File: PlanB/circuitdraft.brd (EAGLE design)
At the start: 24 x 43 mm, 20 parts, among them Q1 16 MHz

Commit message: added biggnd and bigpower for large traces
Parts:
- added BRIDGE1, BRIDGE2, BRIDGE3: (no value), rcl:M0805
- moved CHARGER 3.70 mm to (16.6, 35.1)
- moved LED 2.00 mm to (23.2, 29.6)
- moved BUTTON 1.80 mm to (23.2, 33.5)
- turned SERVO1 to 180 degrees
- turned SERVO2 to 180 degrees
- turned SERVO3 to 180 degrees
- turned SERVO4 to 180 degrees
- turned SERVO5 to 180 degrees
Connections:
- new net BIGGND: BRIDGE3.1, CHARGER.3, REGIN.2, REGOUT.3, SERVO1.3, SERVO2.3, SERVO3.3, SERVO4.3, SERVO5.3
- new net BIGPOWER: BRIDGE1.1, REGOUT.2, SERVO1.2, SERVO2.2, SERVO3.2, SERVO4.2, SERVO5.2
- new net N$9: BRIDGE2.2, U$1.36
- net GND: now also BRIDGE3.2; no longer CHARGER.3, REGIN.2, REGOUT.3, SERVO1.3, SERVO2.3, SERVO3.3, SERVO4.3, SERVO5.3
- net POWER: now also BRIDGE1.2; no longer REGOUT.2, SERVO1.2, SERVO2.2, SERVO3.2, SERVO4.2, SERVO5.2
- net VBAT: now also BRIDGE2.1; no longer U$1.36
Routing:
- net BIGGND: track 0.00 -> 79.7 mm
- net BIGPOWER: track 0.00 -> 55.7 mm, vias 0 -> 1
- net INTERRUPT: track 18.7 -> 54.2 mm, vias 0 -> 2
- net POWER: track 88.8 -> 56.9 mm, vias 1 -> 0
- net SIGNAL3: track 49.7 -> 28.8 mm, vias 0 -> 1
- net SIGNAL2: track 57.7 -> 37.5 mm
- net VBUS: track 21.8 -> 40.0 mm, vias 1 -> 2
- net N$9: track 0.00 -> 7.01 mm
- net DATAIN: track 23.6 -> 18.2 mm
- net RST: track 14.0 -> 19.1 mm, vias 0 -> 3
- net GND: track 0.00 -> 4.90 mm
- net SIGNAL4: track 45.9 -> 50.7 mm
- net SIGNAL5: track 23.4 -> 19.1 mm, vias 1 -> 2
- net N$2: track 6.57 -> 9.69 mm
- net SCK: track 12.4 -> 15.2 mm
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
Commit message: more ajustments
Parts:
- removed BRIDGE3: (no value), rcl:M0805
- removed Q1: 16 MHz, crystal:HC49U
- removed REGIN, REGOUT: (no value), pinhead:1X03
- added REGGNDIN, REGGNDOUT, REGVIN, REGVOUT: (no value), pinhead:1X01
- added Y1: CY16BPS, SamacSys_Parts:CY16BPS
- moved R1 18.3 mm to (19.2, 35.8), turned to 270 degrees
- moved R2 17.9 mm to (16.6, 35.5), turned to 270 degrees
- moved USB 17.7 mm to (7.37, 37.0)
- moved C1 15.6 mm to (16.6, 27.6), turned to 0 degrees
- moved C3 15.3 mm to (27.4, 12.5), turned to 180 degrees
- moved BRIDGE2 13.4 mm to (14.5, 40.3), turned to 270 degrees
- moved BRIDGE1 12.1 mm to (28.4, 2.80), turned to 90 degrees
- moved SERVO1 11.1 mm to (9.60, 28.9)
- moved SERVO2 11.1 mm to (9.60, 25.6)
- moved SERVO3 11.1 mm to (9.60, 22.4)
- moved SERVO4 11.1 mm to (9.60, 19.1)
- moved SERVO5 11.1 mm to (9.60, 15.8)
- moved CHARGER 5.44 mm to (11.5, 37.0)
- moved LED 3.26 mm to (25.3, 27.1), turned to 315 degrees
- moved C2 1.78 mm to (28.6, 7.78)
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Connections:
- removed net BIGGND: BRIDGE3.1, CHARGER.3, REGIN.2, REGOUT.3, SERVO1.3, SERVO2.3, SERVO3.3, SERVO4.3, SERVO5.3
- net BIGPOWER: now also REGVOUT.1; no longer REGOUT.2
- net GND: now also CHARGER.3, REGGNDIN.1, REGGNDOUT.1, SERVO1.3, SERVO2.3, SERVO3.3, SERVO4.3, SERVO5.3, U$1.15, U$1.35, U$1.43; no longer BRIDGE3.2
- net N$5: now also C2.2, U$1.17, Y1.2; no longer C3.2, Q1.1, U$1.16
- net N$6: now also C3.2, U$1.16, Y1.1; no longer C2.2, Q1.3, U$1.17
- net POWER: now also U$1.2
- net VBAT: now also REGVIN.1; no longer REGIN.1
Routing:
- net BIGGND: track 79.7 -> 0.00 mm
- net SIGNAL4: track 50.7 -> 13.6 mm, vias 1 -> 0
- net INTERRUPT: track 54.2 -> 29.4 mm, vias 2 -> 0
- net SIGNAL2: track 37.5 -> 14.6 mm, vias 2 -> 0
- net BIGPOWER: track 55.7 -> 38.9 mm, vias 1 -> 0
- net SIGNAL1: track 38.2 -> 21.5 mm, vias 1 -> 0
- net SIGNAL3: track 28.8 -> 13.4 mm
- net N$4: track 3.67 -> 18.5 mm, vias 0 -> 1
- net POWER: track 56.9 -> 69.8 mm, vias 0 -> 2
- net VBUS: track 40.0 -> 29.8 mm, vias 2 -> 0
- net MISO: track 9.74 -> 19.2 mm, vias 1 -> 0
- net N$9: track 7.01 -> 16.4 mm, vias 0 -> 2
- net N$1: track 26.0 -> 35.4 mm, vias 3 -> 1
- net VBAT: track 26.9 -> 17.7 mm
- net N$2: track 9.69 -> 18.5 mm, vias 0 -> 1
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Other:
- board size 24 x 43 mm -> 25 x 43 mm

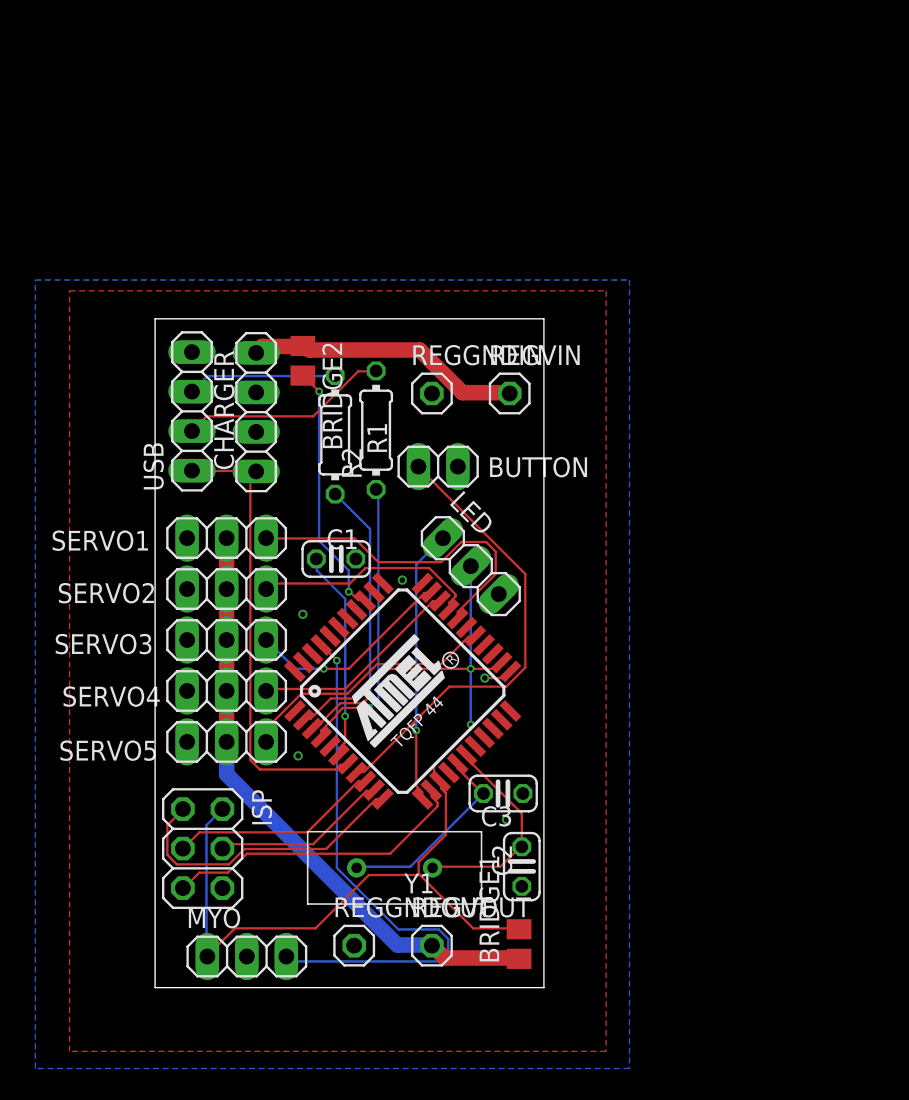
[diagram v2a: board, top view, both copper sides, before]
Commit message: refined board and fixed locations and orintations
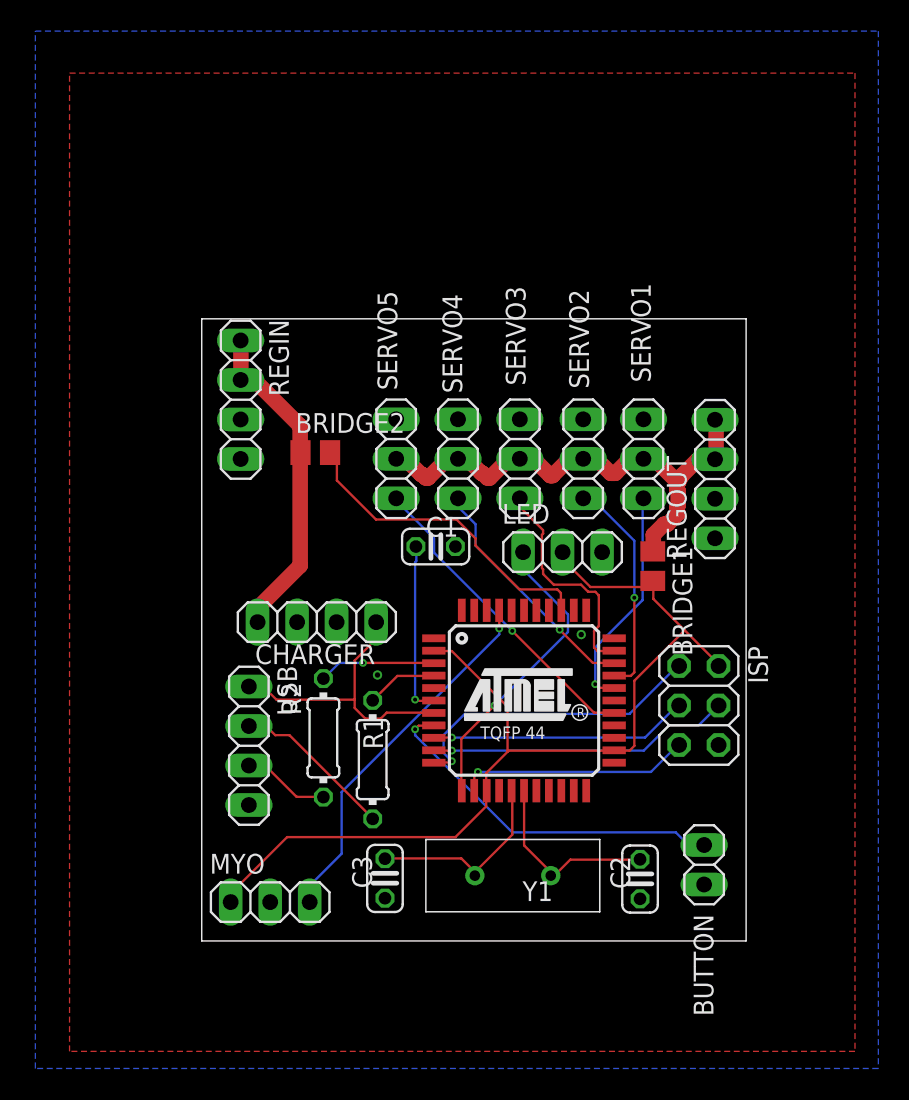
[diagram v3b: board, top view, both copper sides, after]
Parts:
- removed REGGNDIN, REGGNDOUT, REGVIN, REGVOUT: (no value), pinhead:1X01
- added REGIN, REGOUT: (no value), pinhead:1X04
- moved ISP 33.2 mm to (40.0, 18.1)
- moved BUTTON 30.8 mm to (40.3, 7.90), turned to 270 degrees
- moved SERVO1 27.3 mm to (36.4, 34.0), turned to 90 degrees
- moved BRIDGE1 25.8 mm to (37.0, 27.1), turned to 270 degrees
- moved SERVO2 24.4 mm to (32.5, 34.0), turned to 90 degrees
- moved SERVO3 22.2 mm to (28.4, 34.0), turned to 90 degrees
- moved USB 21.8 mm to (11.0, 15.6), turned to 270 degrees
- moved SERVO5 21.2 mm to (20.5, 34.0), turned to 90 degrees
- moved R1 21.2 mm to (19.0, 14.7), turned to 90 degrees
- moved SERVO4 21.1 mm to (24.5, 34.0), turned to 90 degrees
- moved R2 19.5 mm to (15.8, 16.1), turned to 90 degrees
- moved CHARGER 14.1 mm to (15.4, 23.5), turned to 180 degrees
- moved C3 9.36 mm to (19.8, 7.02), turned to 90 degrees
- moved U$1 7.82 mm to (28.7, 18.5), turned to 0 degrees
- moved C2 7.64 mm to (36.2, 6.98)
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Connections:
- net BIGPOWER: now also REGOUT.3, REGOUT.4; no longer REGVOUT.1
- net GND: now also REGIN.3, REGIN.4, REGOUT.1, REGOUT.2; no longer REGGNDIN.1, REGGNDOUT.1
- net VBAT: now also REGIN.1, REGIN.2; no longer REGVIN.1
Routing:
- net N$4: track 18.5 -> 4.58 mm, vias 1 -> 0
- net N$1: track 35.4 -> 23.8 mm
- net VBUS: track 29.8 -> 18.8 mm
- net N$2: track 18.5 -> 7.52 mm
- net MOSI: track 11.3 -> 19.5 mm, vias 0 -> 1
- net SIGNAL1: track 21.5 -> 14.6 mm, vias 0 -> 1
- net INTERRUPT: track 29.4 -> 23.2 mm, vias 0 -> 1
- net BIGPOWER: track 38.9 -> 33.4 mm
- net POWER: track 69.8 -> 64.3 mm, vias 2 -> 0
- net RST: track 19.8 -> 15.0 mm, vias 0 -> 1
- net N$9: track 16.4 -> 20.8 mm, vias 2 -> 0
- net D-: track 9.63 -> 5.63 mm
- net VBAT: track 17.7 -> 21.4 mm
- net SIGNAL5: track 16.7 -> 20.4 mm, vias 0 -> 1
- net SCK: track 13.5 -> 16.7 mm, vias 0 -> 1
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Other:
- board size 25 x 43 mm -> 35 x 40 mm

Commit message: final refinement
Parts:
- C1: device rcl:C025-024X044 -> rcl:C050-024X044
- R1, R2: device rcl:0204/7 -> rcl:0207/10
- moved C1 1.20 mm to (22.2, 27.5)
- moved R1 0.92 mm to (18.8, 15.6)
- moved U$1 0.80 mm to (27.9, 18.5)
- moved R2 0.50 mm to (15.8, 15.6)
- moved BRIDGE1 0.36 mm to (37.3, 26.9)
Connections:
- net INTERRUPT: now also U$1.1; no longer U$1.8
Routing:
- net INTERRUPT: track 23.2 -> 30.9 mm
- net MOSI: track 19.5 -> 23.7 mm
- net VBUS: track 18.8 -> 22.5 mm
- net DATAIN: track 19.4 -> 22.2 mm
- net SCK: track 16.7 -> 17.8 mm
- net N$9: track 20.8 -> 19.7 mm
- net N$4: track 4.58 -> 3.59 mm
- net RST: track 15.0 -> 15.9 mm
- net POWER: track 64.3 -> 63.6 mm
- net D-: track 5.63 -> 6.37 mm
- net SIGNAL3: track 14.6 -> 13.9 mm
- net SIGNAL1: track 14.6 -> 13.9 mm
- net SIGNAL4: track 15.6 -> 15.0 mm
- net N$2: track 7.52 -> 7.16 mm, vias 1 -> 0
- net MISO: track 20.1 -> 20.4 mm, vias 1 -> 2

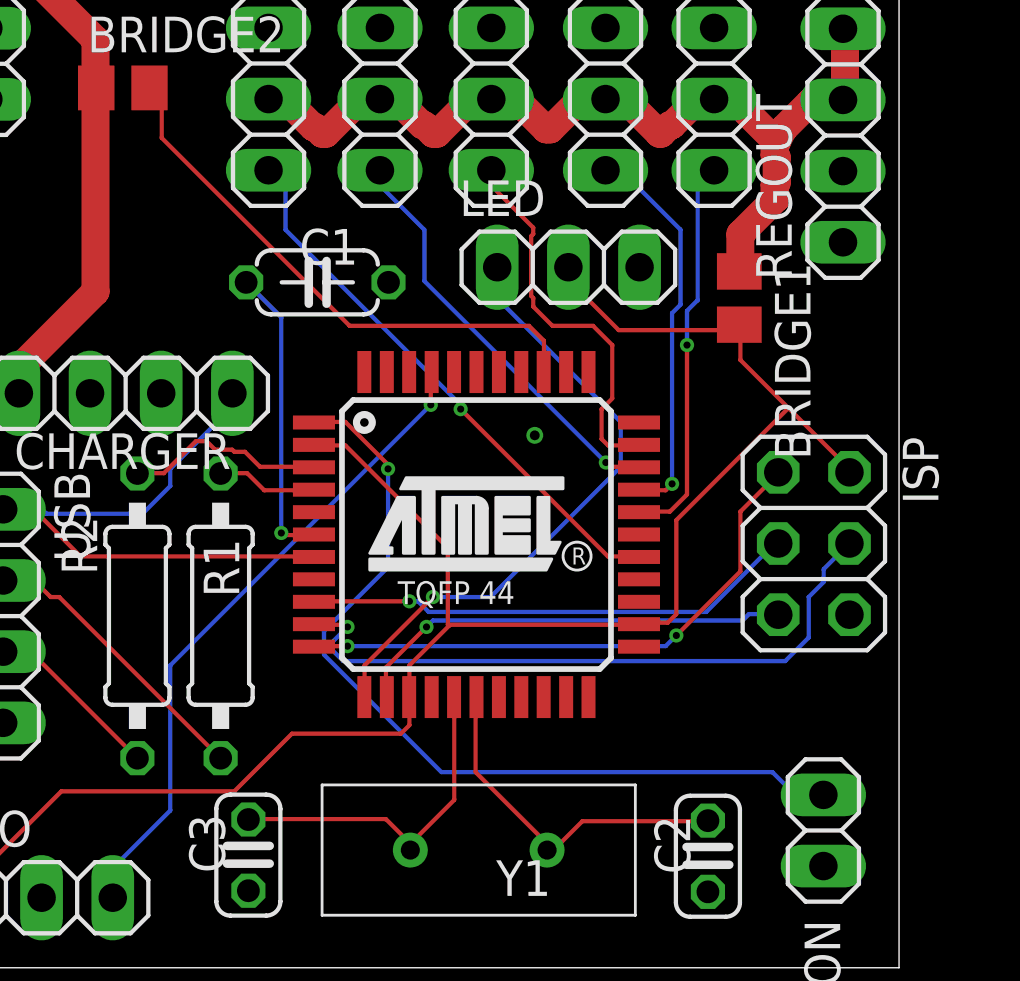
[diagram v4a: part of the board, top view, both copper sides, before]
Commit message: changed some pins to match arduino pins
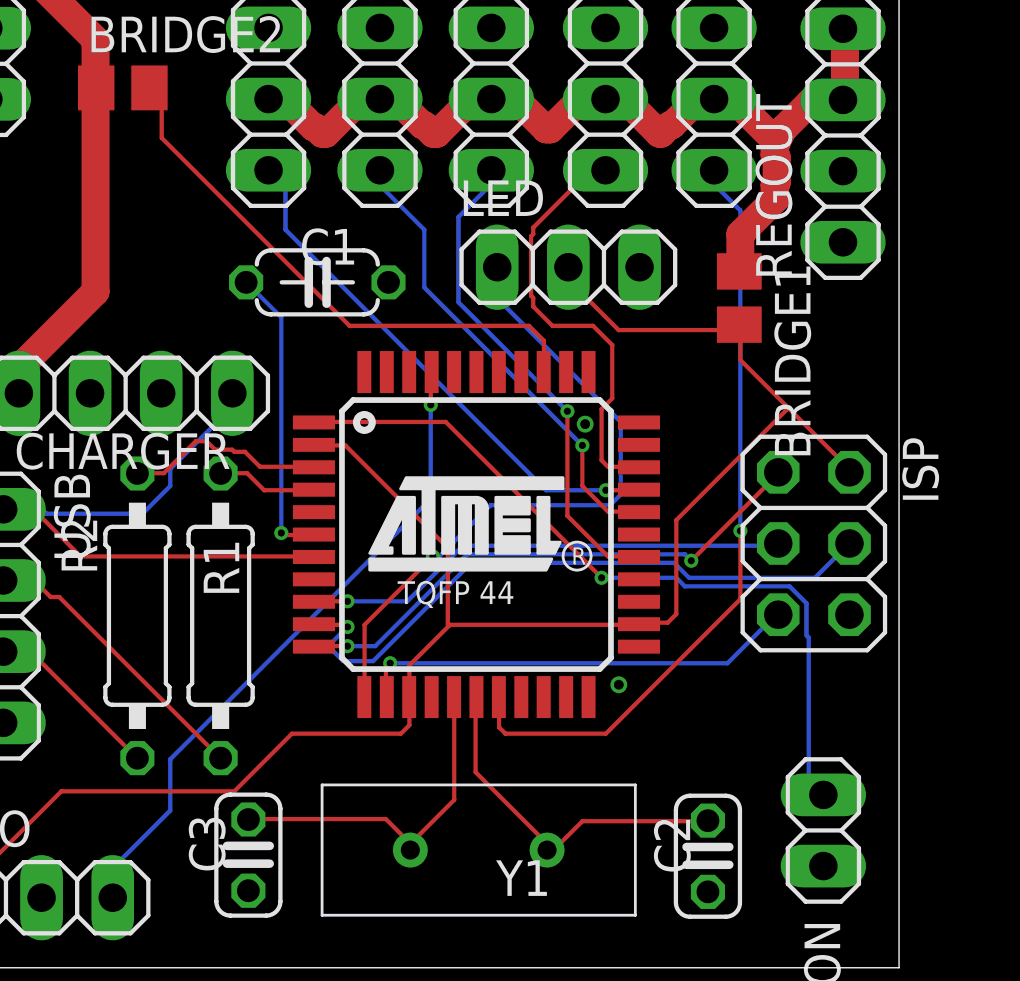
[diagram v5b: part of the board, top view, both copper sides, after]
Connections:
- removed net INT: U$1.25
- removed net SCL: U$1.18
- removed net SDA: U$1.19
- removed net STAT: U$1.26
- net SIGNAL1: now also U$1.18; no longer U$1.29
- net SIGNAL2: now also U$1.31; no longer U$1.30
- net SIGNAL3: now also U$1.27; no longer U$1.32
- net SIGNAL4: now also U$1.29; no longer U$1.31
- net SIGNAL5: now also U$1.30; no longer U$1.27
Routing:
- net SIGNAL1: track 13.9 -> 27.5 mm
- net SIGNAL3: track 13.9 -> 17.6 mm, vias 0 -> 1
- net INTERRUPT: track 30.9 -> 27.4 mm
- net SIGNAL4: track 15.0 -> 16.7 mm
- net DATAIN: track 22.2 -> 23.6 mm
- net SIGNAL2: track 14.1 -> 15.4 mm, vias 1 -> 0
- net SIGNAL5: track 19.9 -> 18.8 mm
- net MISO: track 20.4 -> 19.4 mm
- net MOSI: track 23.7 -> 23.1 mm

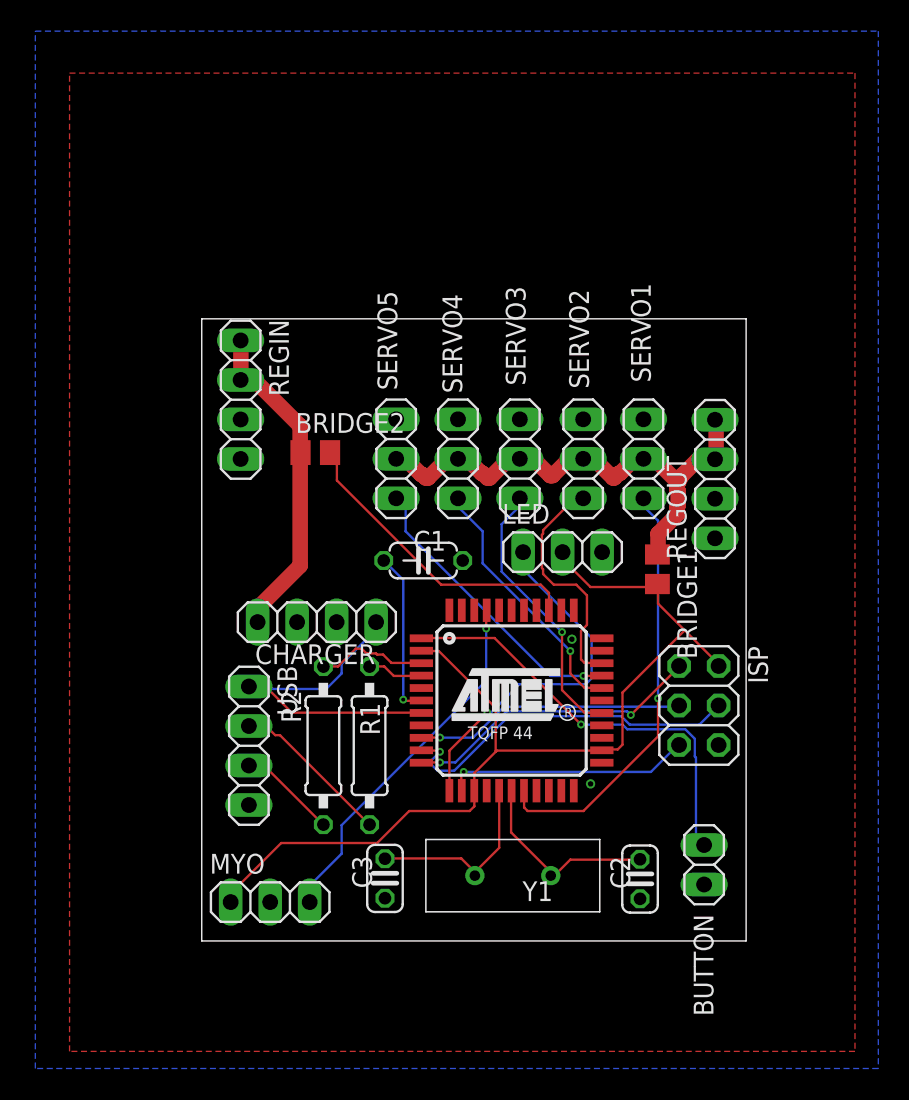
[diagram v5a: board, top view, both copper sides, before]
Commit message: updated
rotated servo ports
removed unnecessary USB things
moved some things around
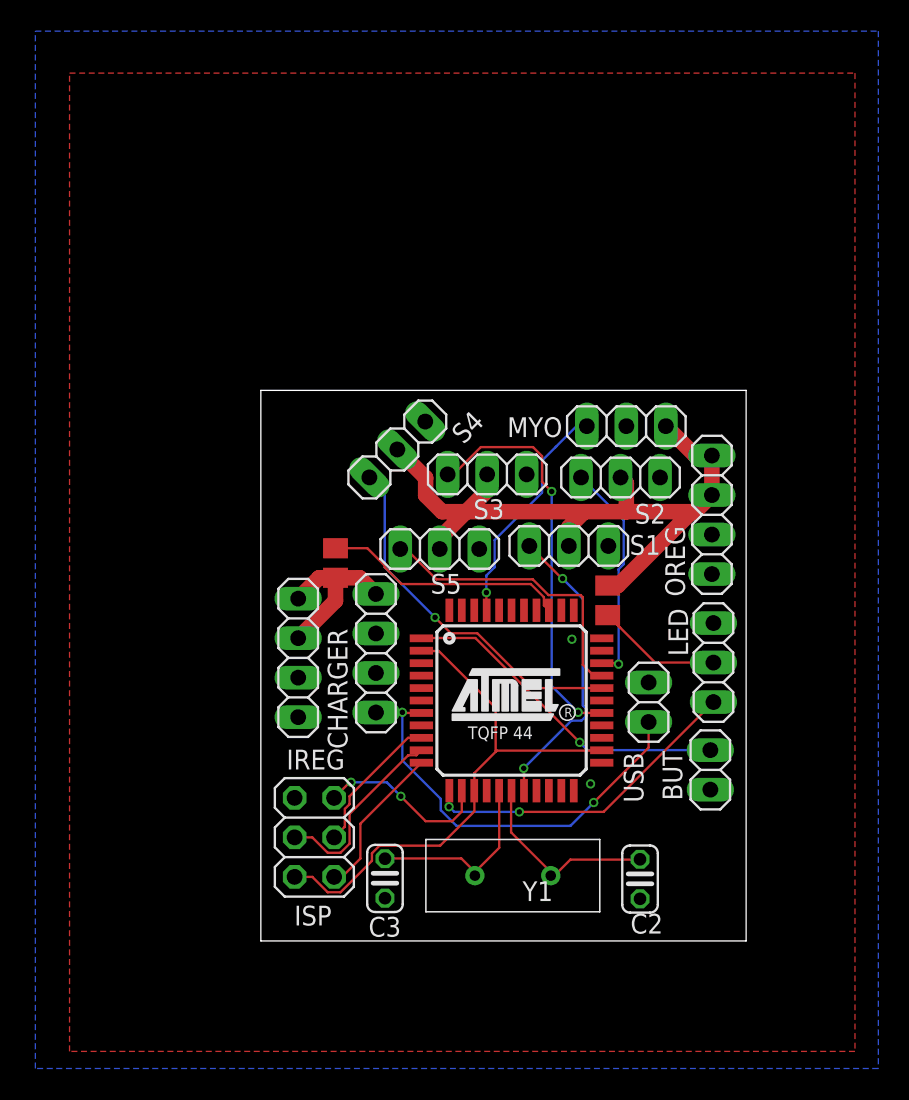
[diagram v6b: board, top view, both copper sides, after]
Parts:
- removed BUTTON: (no value), pinhead:1X02
- removed C1: 1 uF, rcl:C050-024X044
- removed R1, R2: 22 Ohms, rcl:0207/10
- removed REGIN, REGOUT: (no value), pinhead:1X04
- removed SERVO1, SERVO2, SERVO3, SERVO4, SERVO5: (no value), pinhead:1X03
- added BUT: (no value), pinhead:1X02
- added IREG, OREG: (no value), pinhead:1X04
- added S1, S2, S3, S4, S5: (no value), pinhead:1X03
- USB: device pinhead:1X04 -> pinhead:1X02
- moved MYO 38.2 mm to (35.3, 36.1), turned to 180 degrees
- moved ISP 26.1 mm to (15.2, 9.66), turned to 90 degrees
- moved USB 25.9 mm to (36.7, 18.4), turned to 90 degrees
- moved LED 12.0 mm to (40.9, 20.9), turned to 90 degrees
- moved BRIDGE2 7.22 mm to (16.6, 27.3), turned to 90 degrees
- moved CHARGER 4.29 mm to (19.2, 21.5), turned to 90 degrees
- moved BRIDGE1 3.77 mm to (34.1, 24.9)
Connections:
- removed net D+: R1.1, USB.2
- removed net D-: R2.1, USB.3
- removed net N$2: R2.2, U$1.3
- removed net N$3: C1.1, U$1.6
- removed net N$4: R1.2, U$1.4
- net BIGPOWER: now also MYO.1, OREG.3, OREG.4, S1.2, S2.2, S3.2, S4.2, S5.2; no longer REGOUT.3, REGOUT.4, SERVO1.2, SERVO2.2, SERVO3.2, SERVO4.2, SERVO5.2
- net GND: now also BUT.2, IREG.3, IREG.4, OREG.1, OREG.2, S1.3, S2.3, S3.3, S4.3, S5.3, USB.2; no longer BUTTON.2, C1.2, REGIN.3, REGIN.4, REGOUT.1, REGOUT.2, SERVO1.3, SERVO2.3, SERVO3.3, SERVO4.3, SERVO5.3, USB.4
- net INTERRUPT: now also BUT.1; no longer BUTTON.1
- net POWER: no longer MYO.1
- net SIGNAL1: now also S1.1; no longer SERVO1.1
- net SIGNAL2: now also S2.1; no longer SERVO2.1
- net SIGNAL3: now also S3.1; no longer SERVO3.1
- net SIGNAL4: now also S4.1; no longer SERVO4.1
- net SIGNAL5: now also S5.1; no longer SERVO5.1
- net VBAT: now also IREG.1, IREG.2; no longer REGIN.1, REGIN.2
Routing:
- net POWER: track 63.6 -> 44.0 mm
- net BIGPOWER: track 33.7 -> 48.0 mm
- net N$3: track 10.7 -> 0.00 mm, vias 1 -> 0
- net MOSI: track 23.1 -> 12.5 mm, vias 1 -> 0
- net VBAT: track 21.4 -> 10.9 mm
- net D+: track 10.4 -> 0.00 mm
- net MISO: track 19.4 -> 10.0 mm, vias 2 -> 0
- net N$1: track 23.5 -> 15.0 mm
- net SIGNAL3: track 17.6 -> 26.1 mm, vias 1 -> 2
- net SCK: track 17.4 -> 9.28 mm, vias 1 -> 0
- net SIGNAL1: track 27.5 -> 19.4 mm, vias 1 -> 2
- net N$2: track 7.16 -> 0.00 mm
- net SIGNAL4: track 16.7 -> 23.4 mm
- net D-: track 6.37 -> 0.00 mm
- net INTERRUPT: track 27.4 -> 21.6 mm
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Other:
- board size 35 x 40 mm -> 31.2 x 35.4 mm
